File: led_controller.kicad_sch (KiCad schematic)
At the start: 55 parts, among them J1 Screw_Terminal_01x02, J10 Conn_01x03, J2 SJ-3524-SMT, J3 Conn_01x03, J4 Conn_01x03, J5 Conn_01x03, J6 Conn_01x03, J7 Conn_01x03, J8 Conn_01x03, J9 Conn_01x03, SW1 RotaryEncoder_Switch, U1 MAX9814, U2 74HCT245, U3 Teensy4.0, U4 Adafruit_TFT_1in3_ST7789

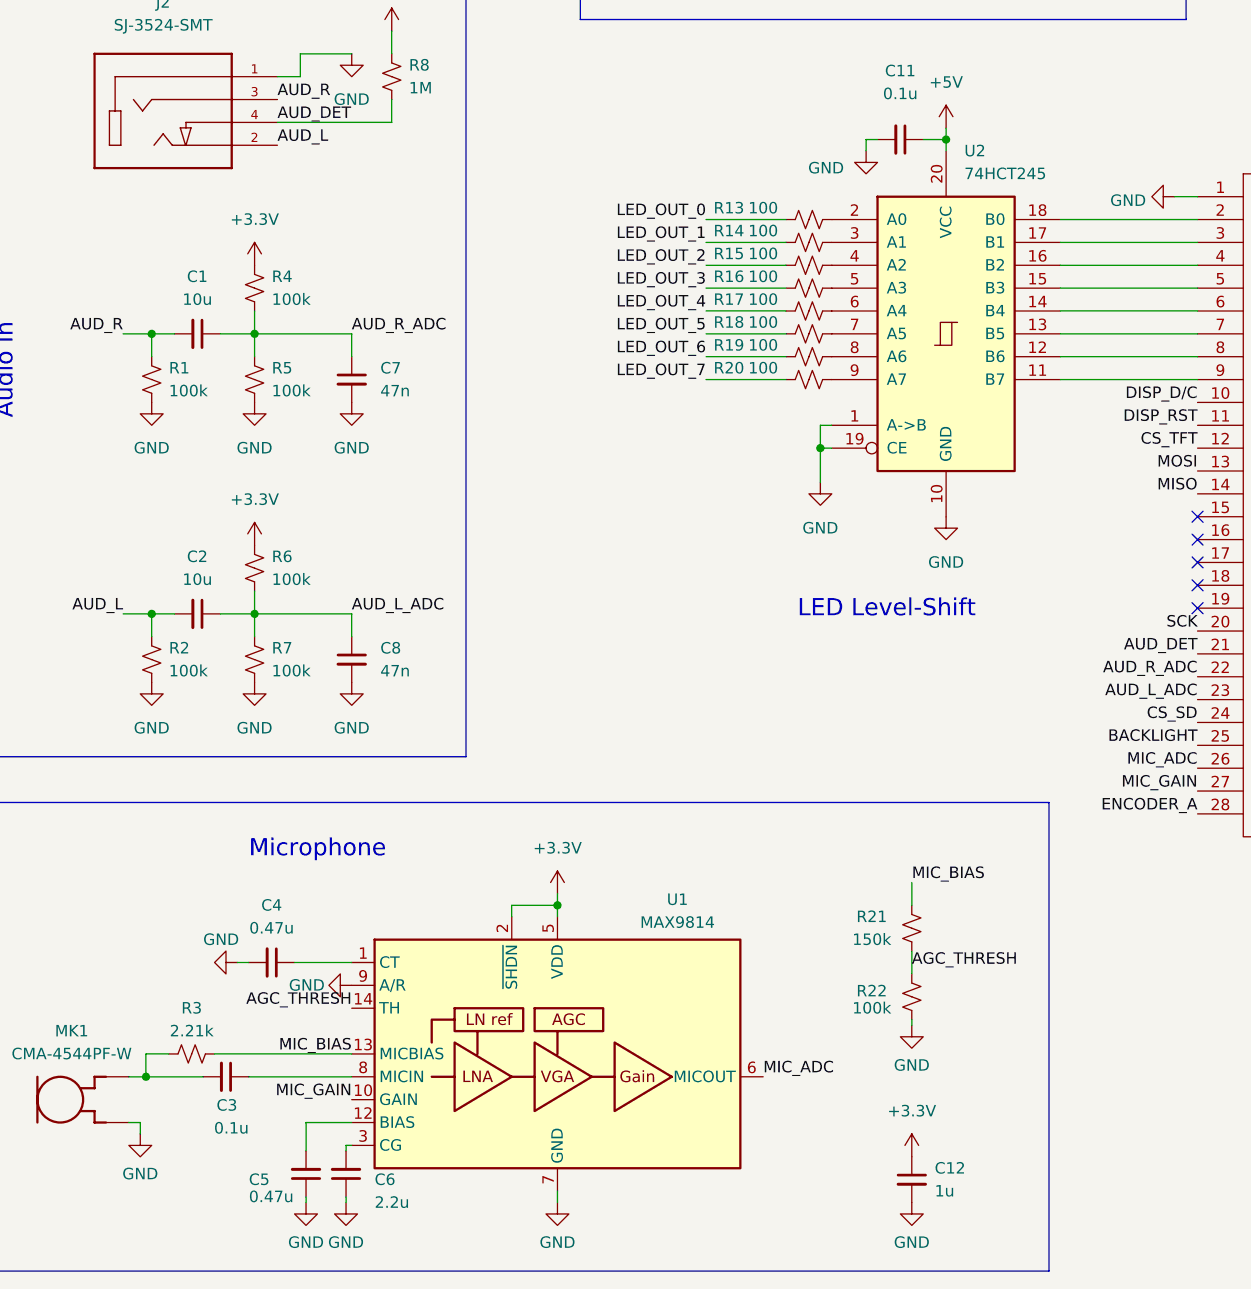
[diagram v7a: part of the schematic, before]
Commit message: Edit symbol fields for PCB assembly
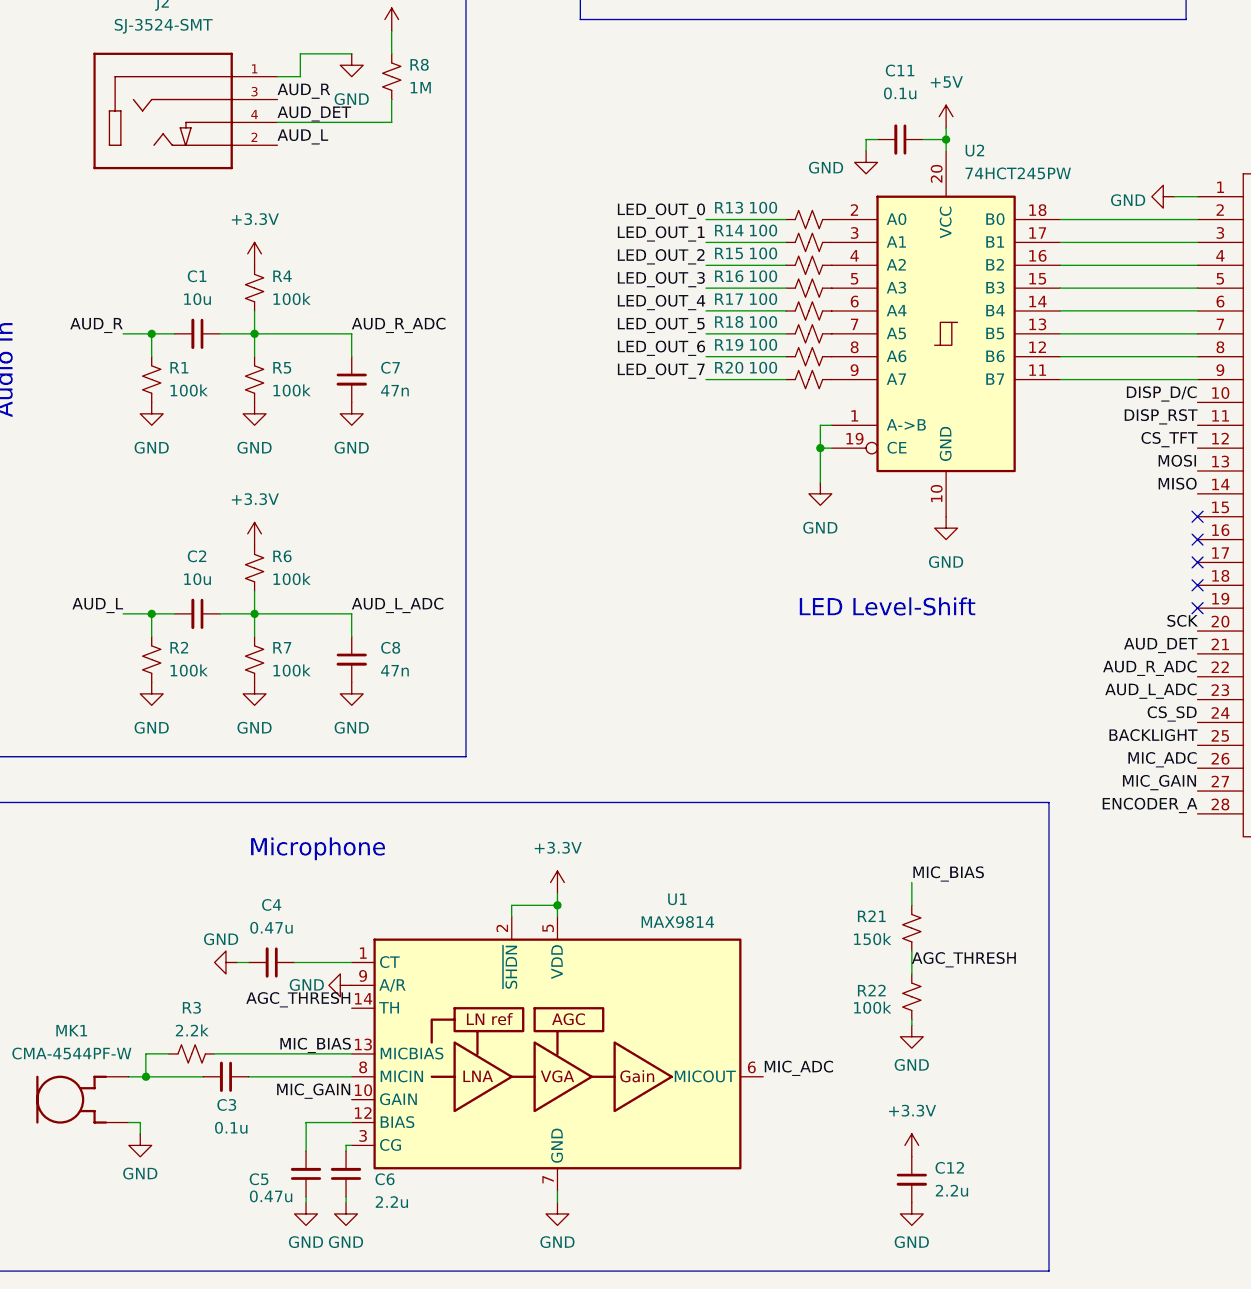
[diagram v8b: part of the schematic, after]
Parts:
- C1, C13, C2, C7, C8, R8: Layer (none) -> F; Package (none) -> 0805
- C10, C9: LCSC Part Number (none) -> C1710; Layer (none) -> B; Package (none) -> 0805
- C11, C3: LCSC Part Number (none) -> C49678; Layer (none) -> B; Package (none) -> 0805
- C12: value 1u -> 2.2u; LCSC Part Number (none) -> C49217; Layer (none) -> B; Package (none) -> 0805
- C4, C5: LCSC Part Number (none) -> C13967; Layer (none) -> B; Package (none) -> 0805
- C6: LCSC Part Number (none) -> C49217; Layer (none) -> B; Package (none) -> 0805
- H1, H2, H3, H4: LCSC Part Number (none) -> N/A; Layer (none) -> N; Package (none) -> N/A
- J1: LCSC Part Number (none) -> N/A; Layer (none) -> F; Package (none) -> N/A
- J10, J3, J4, J5, J6, J7, J8, J9: LCSC Part Number (none) -> N/A; Layer (none) -> F; Package (none) -> JST_PH_1x3_THT
- J2: LCSC Part Number (none) -> N/A; Layer (none) -> F; MF CUI Inc -> (none); PARTREV 1.03 -> (none); Package (none) -> N/A; STANDARD Manufacturer recommendations -> (none)
- MK1: AVAILABILITY Unavailable -> (none); CUI_PURCHASE_URL https://www.cui.com/product/audio/microphones/electret-cond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 -> (none); DESCRIPTION 9.7 mm, Omnidirectional, PCB Mount, 3.0 Vdc, Electret Conde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 -> (none); LCSC Part Number (none) -> N/A; Layer (none) -> F; MF CUI Inc. -> (none); MP CMA-4544PF-W -> (none); PACKAGE 6-DIP-6 CUI -> (none); PRICE None -> (none); Package (none) -> N/A
- R1, R2, R4, R5, R6, R7: LCSC Part Number (none) -> C149504; Layer (none) -> F; Package (none) -> 0805
- R10, R11, R12, R9: LCSC Part Number (none) -> C17414; Layer (none) -> B; Package (none) -> 0805
- R13, R14, R15, R16, R17, R18, R19, R20: LCSC Part Number (none) -> C17408; Layer (none) -> B; Package (none) -> 0805
- R21: LCSC Part Number (none) -> C17470; Layer (none) -> B; Package (none) -> 0805
- R22: LCSC Part Number (none) -> C149504; Layer (none) -> B; Package (none) -> 0805
- R3: value 2.21k -> 2.2k; LCSC Part Number (none) -> C17520; Layer (none) -> B; Package (none) -> 0805
- SW1: LCSC Part Number (none) -> N/A; Layer (none) -> F; Package (none) -> EC11
- U1: LCSC Part Number (none) -> C41714; Layer (none) -> B; Package (none) -> TDFN14
- U2: value 74HCT245 -> 74HCT245PW; LCSC Part Number (none) -> C5980; Layer (none) -> B; Package (none) -> TSSOP20
- U3: LCSC Part Number (none) -> N/A; Layer (none) -> F; Package (none) -> 0.1" 2x14
- U4: LCSC Part Number (none) -> N/A; Layer (none) -> F; Package (none) -> 0.1" 1x11
